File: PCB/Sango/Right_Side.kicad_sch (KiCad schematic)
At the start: 38 parts, among them IC1 W25Q16JVUXIQ, J1 USB_C_Receptacle_USB2.0, J2 AudioJack4, SW1 SW_Push, SW2 SW_Push, U1 RP2040, U2 XC6210B332MR, U5 USBLC6-2P6, U6 USBLC6-2P6, Y1 Crystal_GND24

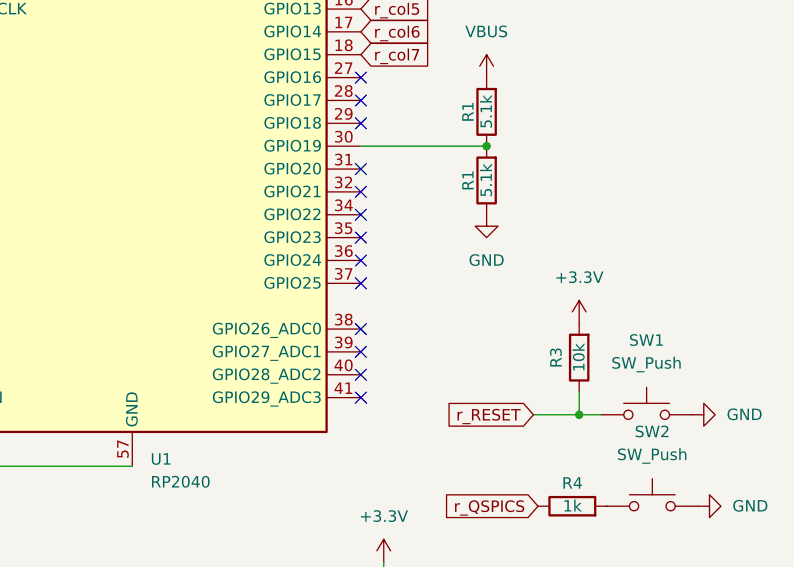
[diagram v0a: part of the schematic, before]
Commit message: Added handdedness pin (GPIO25).
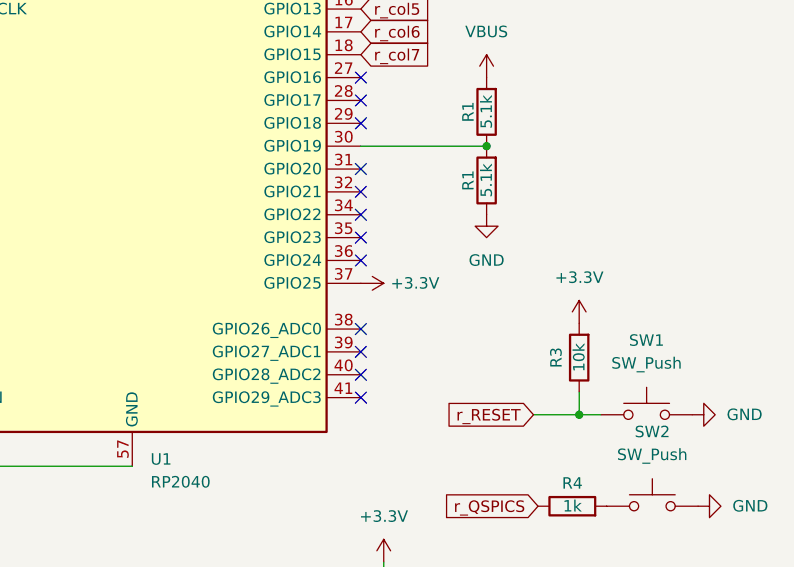
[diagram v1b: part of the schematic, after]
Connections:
- net +3.3V: now also U1.37 (GPIO25)
- no-connect marks 21 -> 20
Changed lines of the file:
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@@
   (no_connect (at 233.68 99.06))
   (no_connect (at 233.68 76.2))
-  (no_connect (at 233.68 93.98))
   (no_connect (at 182.88 99.06))
   (no_connect (at 182.88 96.52))
@@
         )
       )
+    )
+  )
+  (symbol (lib_id "power:+3.3V") (at 233.68 93.98 270) (unit 1)
+    (in_bom yes) (on_board yes) (dnp no) (fields_autoplaced)
+    (property "Reference" "#PWR0114" (at 229.87 93.98 0)
+      (effects (font (size 1.27 1.27)) hide)
+    )
+    (property "Value" "+3.3V" (at 236.982 93.98 90)
+      (effects (font (size 1.27 1.27)) (justify left))
+    )
+    (property "Footprint" "" (at 233.68 93.98 0)
+      (effects (font (size 1.27 1.27)) hide)
+    )
+    (property "Datasheet" "" (at 233.68 93.98 0)
+      (effects (font (size 1.27 1.27)) hide)
+    )
+    (pin "1")
+    (instances
+      (project "Main PCB"
+        (path "/a96e3b6b-3809-4995-a49d-2602f32cc3bc"
+          (reference "#PWR0114") (unit 1)
+        )
+      )
+      (project "Sango"
+        (path "/b3610507-f8cf-4536-91fb-ccd246b0546b"
+          (reference "#PWR010") (unit 1)
+        )
+        (path "/b3610507-f8cf-4536-91fb-ccd246b0546b/8844218a-baae-4d88-93bf-a73f8aae810d"
+          (reference "#PWR087") (unit 1)
+        )
+      )
